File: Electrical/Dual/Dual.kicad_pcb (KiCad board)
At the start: 2 copper layers, 140 x 70 mm, 190 parts, among them J101 01x04, J102 02x04, J103 01x04, J104 01x03, J105 01x03, J106 01x03, J107 01x03, J108 01x03, J109 01x03, J110 01x04, J111 01x04, J112 01x04, J113 01x04, J114 01x03, J115 01x03, J116 01x03, J117 01x03, J201 01x03, J202 01x04, J203 01x03, J204 01x04, J205 01x03, J206 USB_OTG, J207 01x04, J208 01x02, J209 01x04, J210 01x02, J211 01x02, J212 4PostTerm, J213 2PostTerm, J214 2PostTerm, J215 2PostTerm, J216 2PostTerm, J217 2PostTerm, J218 01x02, J219 01x02, Q201 FDC6420C, Q202 FDG1024NZ, Q301 FDC6420C, Q401 FDC6420C, U201 TPD4S012, U202 ACS712ELCTR-05B-T, U203 ACS712ELCTR-05B-T, U204 24LC256, U205 LM2576HVS-ADJ, U206 LM2576HVS-ADJ, x100 02x05, x101 RoutaCell, x102 RoutaCell, x103 RoutaCell, x104 RoutaCell, x105 RoutaCell, x106 RoutaCell, x107 RoutaCell, x108 RoutaCell, x109 RoutaCell, x110 RoutaCell, x111 RoutaCell, x112 RoutaCell, x113 RoutaCell, x114 RoutaCell, x115 RoutaCell, x116 RoutaCell, x117 RoutaCell, x118 RoutaCell, x119 RoutaCell, x120 RoutaCell, x121 RoutaCell, x122 RoutaCell, x123 RoutaCell, x124 RoutaCell, x125 RoutaCell, x126 RoutaCell, x127 RoutaCell, x128 RoutaCell, x129 RoutaCell, x130 RoutaCell, x131 RoutaCell, x132 RoutaCell, x133 RoutaCell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

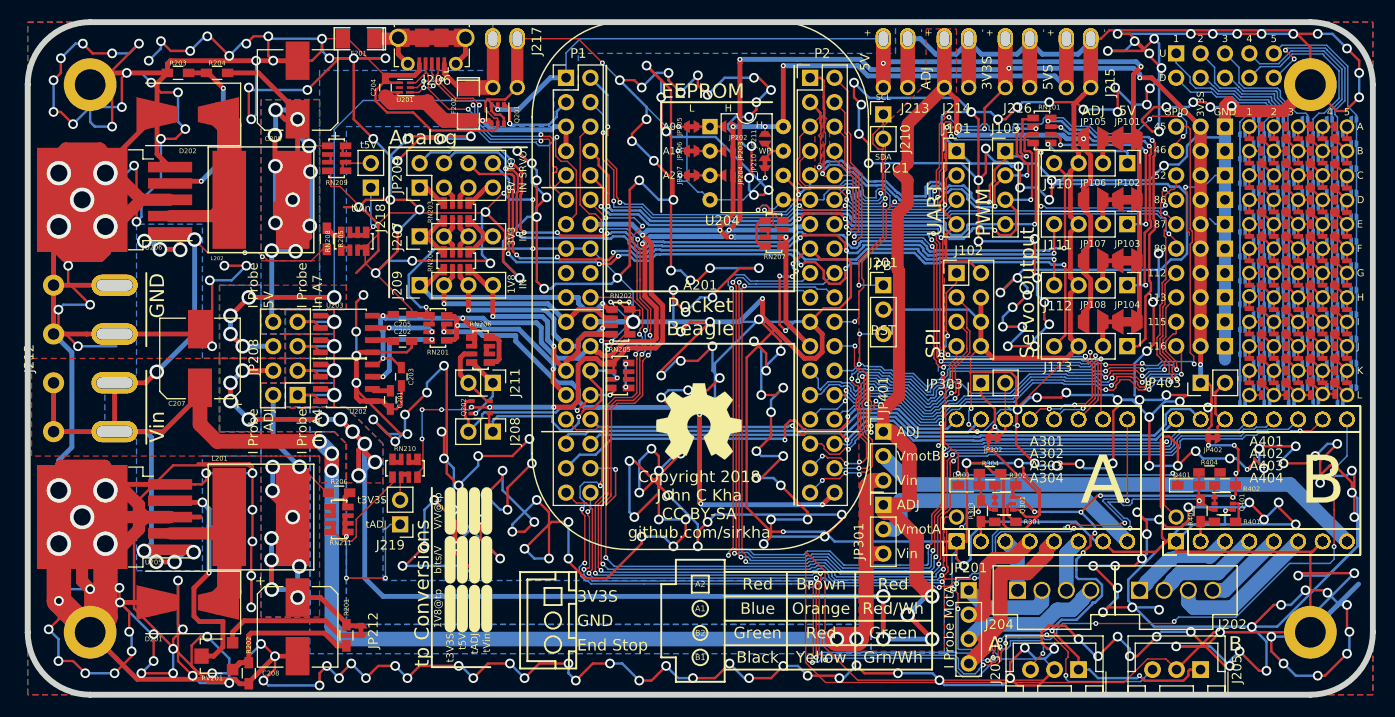
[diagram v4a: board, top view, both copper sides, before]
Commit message: Applied improvements from routing quad board to dual board.
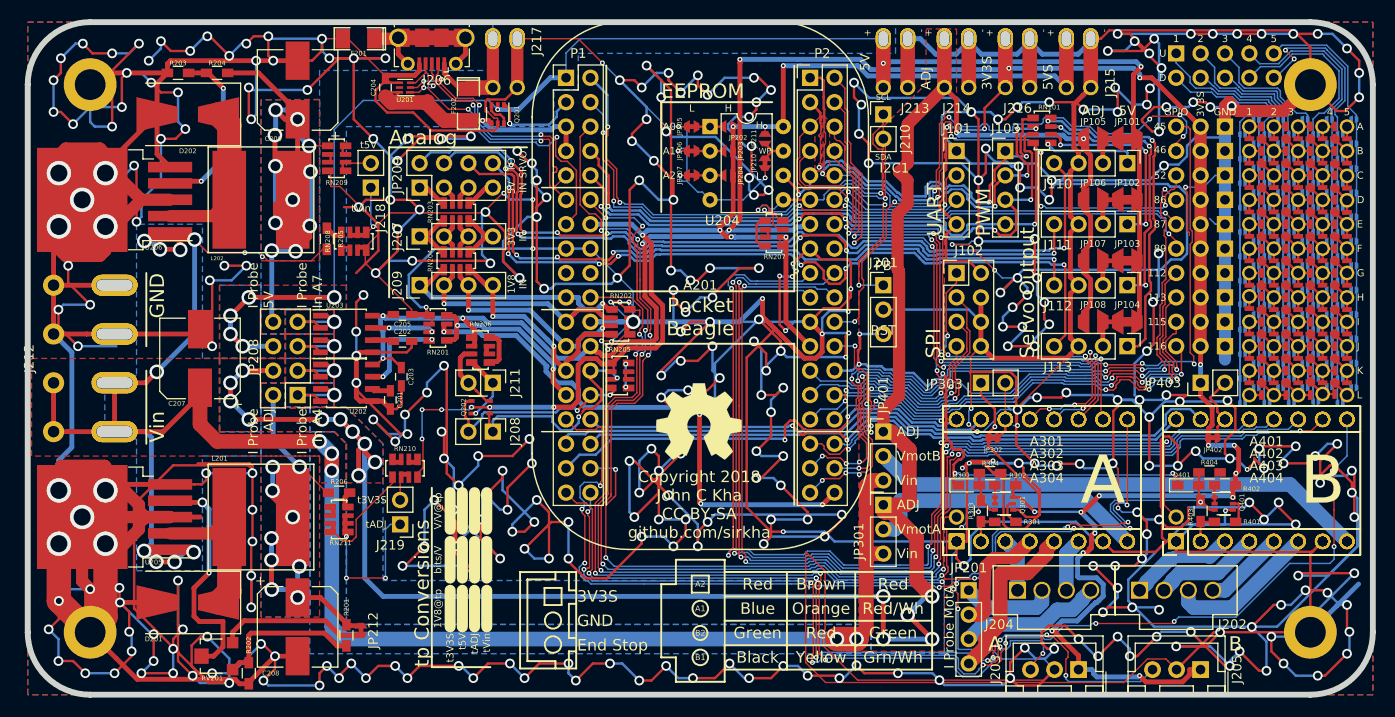
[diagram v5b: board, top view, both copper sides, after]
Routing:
- net GND: track 2759.2 -> 2815.3 mm, vias 381 -> 391
- net RST: track 55.5 -> 64.3 mm
- net 3V3S: track 316.8 -> 325.4 mm, vias 31 -> 30
- net /gpio1_20: track 59.9 -> 58.2 mm
- net /Common/pr1_pru0_pru_r30_07: track 100.9 -> 99.2 mm
- net /Common/i2c1_scl: track 32.0 -> 30.6 mm
- net /spi1_sclk: track 28.8 -> 27.6 mm
- net /spi1_d0: track 23.5 -> 22.3 mm
- net /gpio3_20: track 44.2 -> 43.1 mm
- net /Common/ain3: track 26.5 -> 25.4 mm
- net /Common/gpio0_4: track 126.6 -> 125.5 mm
- net /spi1_d1: track 28.7 -> 29.8 mm, vias 2 -> 3
- net /Common/i2c1_sda: track 26.4 -> 25.5 mm
- net /Common/ain2: track 23.9 -> 23.0 mm
- net 5VS: track 134.2 -> 133.3 mm
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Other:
- net class Default: clearance 0.1524 -> 0.152146
- net class Minimum: clearance 0.1524 -> 0.152146
- net class PowerL: clearance 5.08 -> 0.152146
- net class PowerM: clearance 2.54 -> 0.152146
- net class PowerS: clearance 1.524 -> 0.152146
- rule trace_clearance: 0.1524 -> 0.152146
- rule trace_min: 0.152375 -> 0.14986

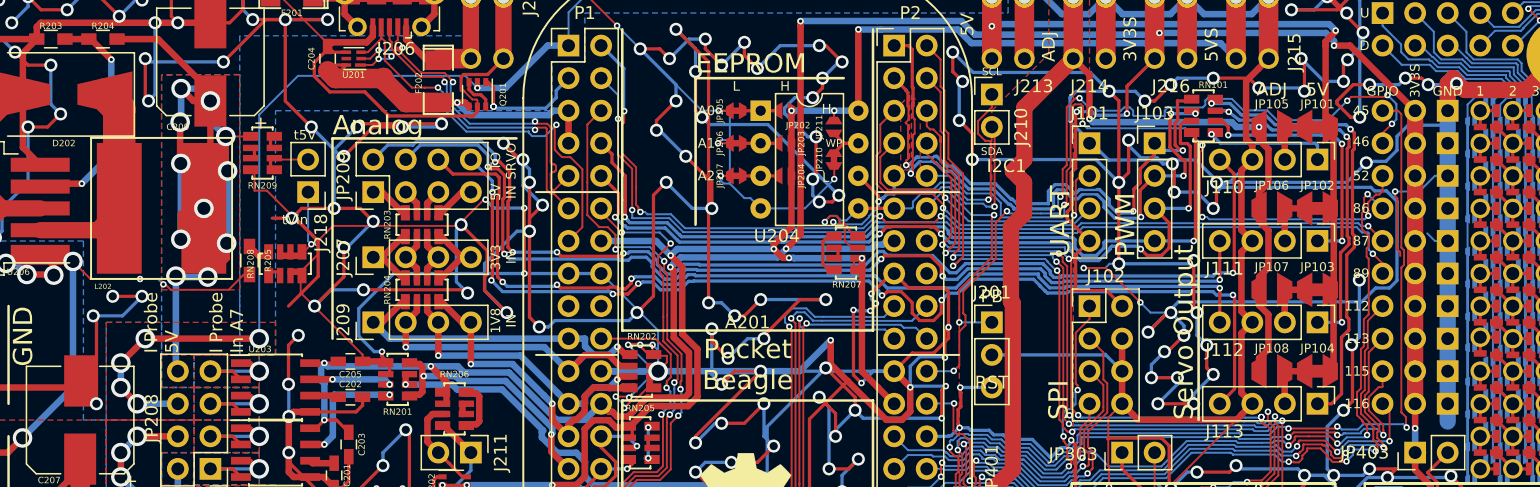
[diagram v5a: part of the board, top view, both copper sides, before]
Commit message: DRC Erros fixed.
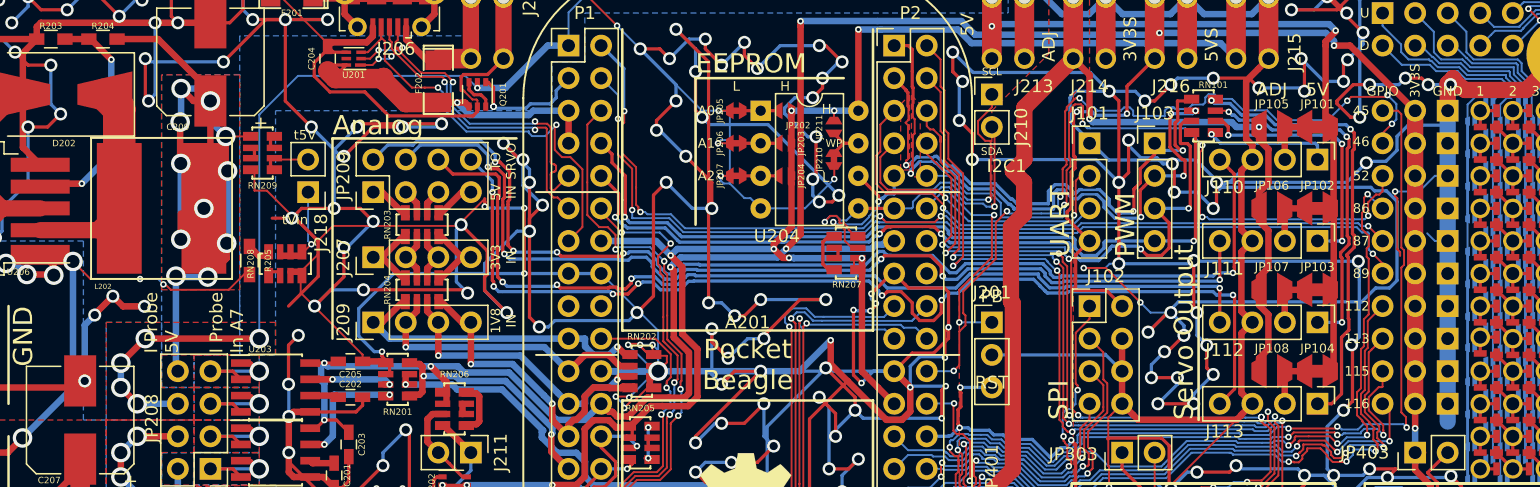
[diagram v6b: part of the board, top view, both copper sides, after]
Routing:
- net GND: track 2815.3 -> 2840.7 mm, vias 391 -> 395
- net (no net): track 13.7 -> 0.00 mm, vias 4 -> 0
- net /gpio1_14: track 62.7 -> 63.5 mm
- net Net-(J112-Pad1): track 29.2 -> 28.4 mm
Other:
- net class Default: clearance 0.152146 -> 0.1524
- net class Minimum: clearance 0.152146 -> 0.1524
- net class PowerL: clearance 0.152146 -> 0.1524
- net class PowerM: clearance 0.152146 -> 0.1524
- net class PowerS: clearance 0.152146 -> 0.1524
- rule trace_clearance: 0.152146 -> 0.1524

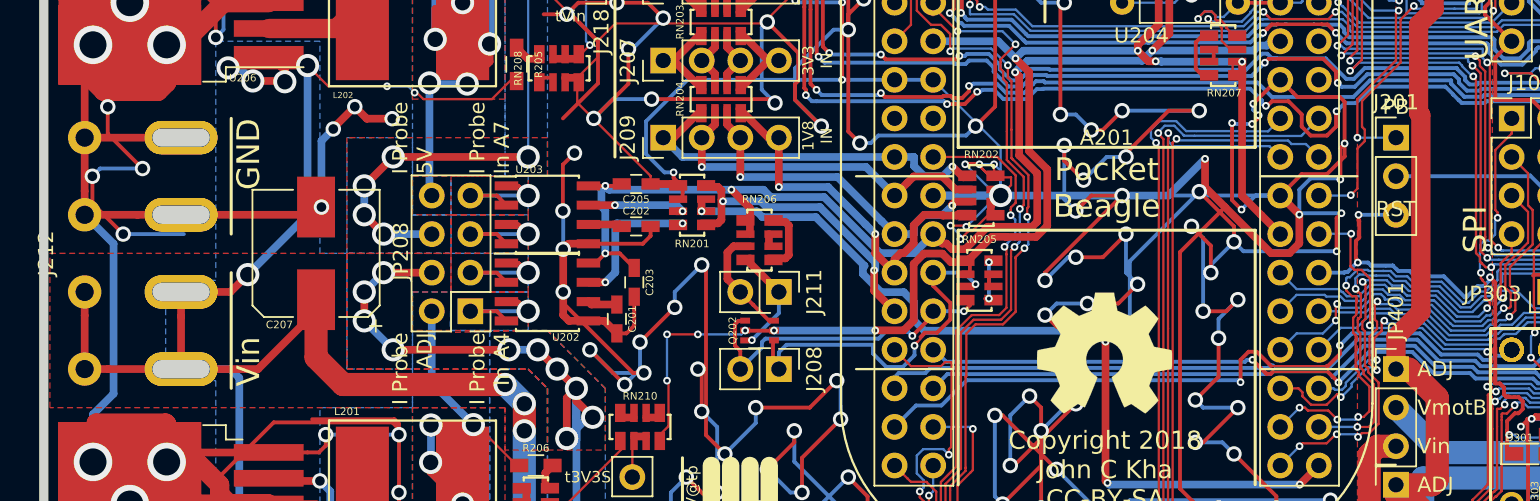
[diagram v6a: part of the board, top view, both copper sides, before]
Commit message: Fixed silkscreen errors and other minor improvements to trace layouts.
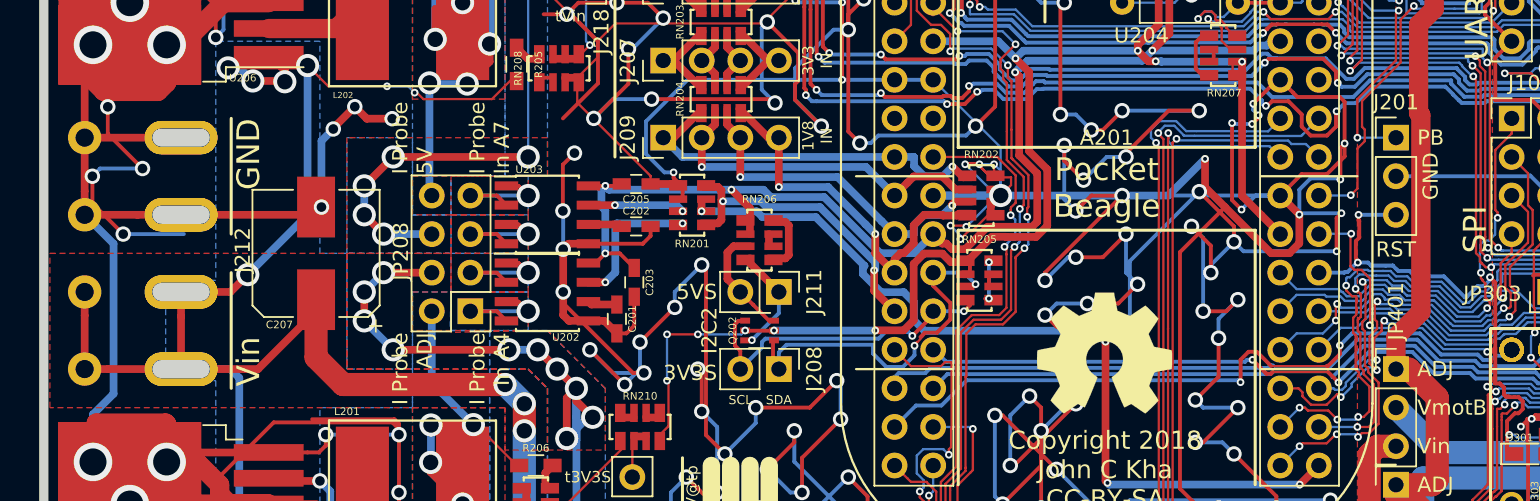
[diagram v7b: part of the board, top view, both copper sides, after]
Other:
- board text added: "I2C2"
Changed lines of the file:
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@@
   (general
     (links 628)
-    (no_connects 0)
-    (area 29.695199 64.695199 170.304801 135.304801)
+    (no_connects 4)
+    (area 13.150001 61.9886 171.057639 147.700001)
     (thickness 1.6)
-    (drawings 284)
+    (drawings 290)
     (tracks 5789)
     (zones 0)
@@
   )
   (setup
-    (last_trace_width 0.1524)
+    (last_trace_width 0.254)
     (user_trace_width 0.1524)
     (user_trace_width 0.254)
@@
   (module footprints:TerminalBlock_Custom_1x04P5.08mm (layer F.Cu)
     (at 36.5 100 270)
-    (fp_text reference J212 (at 0 6.35 270) (layer F.SilkS)
+    (fp_text reference J212 (at -0.21844 -6.604 270) (layer F.SilkS)
       (effects (font (size 1 1) (thickness 0.15)))
     )
@@
     )
   )
+  (gr_text 5VS (at 74.346 102.54) (layer F.SilkS)
+    (effects (font (size 1 1) (thickness 0.2)) (justify right))
+  )
+  (gr_text 3V3S (at 74.346 107.874) (layer F.SilkS)
+    (effects (font (size 1 1) (thickness 0.2)) (justify right))
+  )
+  (gr_text SCL (at 75.87 109.652) (layer F.SilkS)
+    (effects (font (size 0.6 0.6) (thickness 0.15)))
+  )
+  (gr_text SDA (at 78.41 109.652) (layer F.SilkS)
+    (effects (font (size 0.6 0.6) (thickness 0.15)))
+  )
+  (gr_text I2C2 (at 73.838 105.08 90) (layer F.SilkS)
+    (effects (font (size 1 1) (thickness 0.2)))
+  )
+  (gr_text GND (at 121.336 94.92 90) (layer F.SilkS)
+    (effects (font (size 1 1) (thickness 0.2)))
+  )
   (gr_text "Prototyping area inspired by Routaboard.\nroutaboard.com" (at 168.834 110.414) (layer B.SilkS)
     (effects (font (size 1.5 1.5) (thickness 0.3)) (justify left mirror))
@@
     (effects (font (size 0.6 0.6) (thickness 0.15)))
   )
-  (gr_text PB (at 119.05 90.348) (layer F.SilkS)
+  (gr_text PB (at 121.336 92.38) (layer F.SilkS)
     (effects (font (size 1 1) (thickness 0.2)))
   )
@@
   )
   (gr_line (start 135.179 100) (end 135.179 78.41) (layer F.SilkS) (width 0.2))
-  (gr_text RST (at 119.05 97.079) (layer F.SilkS)
+  (gr_text RST (at 119.05 99.746) (layer F.SilkS)
     (effects (font (size 1 1) (thickness 0.2)))
   )
@@
     (connect_pads (clearance 0.25146))
     (min_thickness 0.25146)
-    (fill yes (arc_segments 16) (thermal_gap 0.254) (thermal_bridge_width 1.524))
+    (fill (arc_segments 16) (thermal_gap 0.254) (thermal_bridge_width 1.524))
     (polygon
       (pts
@@
     (connect_pads (clearance 0.25146))
     (min_thickness 0.25146)
-    (fill yes (arc_segments 16) (thermal_gap 0.254) (thermal_bridge_width 1.524))
+    (fill (arc_segments 16) (thermal_gap 0.254) (thermal_bridge_width 1.524))
     (polygon
       (pts
@@
     (connect_pads (clearance 0.25146))
     (min_thickness 0.25146)
-    (fill yes (arc_segments 16) (thermal_gap 0.254) (thermal_bridge_width 1.524))
+    (fill (arc_segments 16) (thermal_gap 0.254) (thermal_bridge_width 1.524))
     (polygon
       (pts
@@
     (connect_pads (clearance 0.25146))
     (min_thickness 0.25146)
-    (fill yes (arc_segments 16) (thermal_gap 0.254) (thermal_bridge_width 1.524))
+    (fill (arc_segments 16) (thermal_gap 0.254) (thermal_bridge_width 1.524))
     (polygon
       (pts
@@
     (connect_pads (clearance 0.25146))
     (min_thickness 0.25146)
-    (fill yes (arc_segments 16) (thermal_gap 0.254) (thermal_bridge_width 1.524))
+    (fill (arc_segments 16) (thermal_gap 0.254) (thermal_bridge_width 1.524))
     (polygon
       (pts
@@
     (connect_pads (clearance 0.25146))
     (min_thickness 0.25146)
-    (fill yes (arc_segments 16) (thermal_gap 0.254) (thermal_bridge_width 1.524))
+    (fill (arc_segments 16) (thermal_gap 0.254) (thermal_bridge_width 1.524))
     (polygon
       (pts
@@
     (connect_pads (clearance 0.1778))
     (min_thickness 0.1778)
-    (fill yes (arc_segments 16) (thermal_gap 0.254) (thermal_bridge_width 0.254))
+    (fill (arc_segments 16) (thermal_gap 0.254) (thermal_bridge_width 0.254))
     (polygon
       (pts
@@
     (connect_pads (clearance 0.1778))
     (min_thickness 0.1778)
-    (fill yes (arc_segments 16) (thermal_gap 0.254) (thermal_bridge_width 0.254))
+    (fill (arc_segments 16) (thermal_gap 0.254) (thermal_bridge_width 0.254))
     (polygon
       (pts
@@
     (connect_pads (clearance 0.25146))
     (min_thickness 0.25146)
-    (fill yes (arc_segments 16) (thermal_gap 0.254) (thermal_bridge_width 1.524))
+    (fill (arc_segments 16) (thermal_gap 0.254) (thermal_bridge_width 1.524))
     (polygon
       (pts
@@
     (connect_pads (clearance 0.25146))
     (min_thickness 0.25146)
-    (fill yes (arc_segments 16) (thermal_gap 0.254) (thermal_bridge_width 1.524))
+    (fill (arc_segments 16) (thermal_gap 0.254) (thermal_bridge_width 1.524))
     (polygon
       (pts
@@
     (connect_pads (clearance 0.25146))
     (min_thickness 0.25146)
-    (fill yes (arc_segments 16) (thermal_gap 0.254) (thermal_bridge_width 1.524))
+    (fill (arc_segments 16) (thermal_gap 0.254) (thermal_bridge_width 1.524))
     (polygon
       (pts
@@
     (connect_pads (clearance 0.25146))
     (min_thickness 0.25146)
-    (fill yes (arc_segments 16) (thermal_gap 0.254) (thermal_bridge_width 1.524))
+    (fill (arc_segments 16) (thermal_gap 0.254) (thermal_bridge_width 1.524))
     (polygon
       (pts
@@
     (connect_pads (clearance 0.25146))
     (min_thickness 0.25146)
-    (fill yes (arc_segments 16) (thermal_gap 0.254) (thermal_bridge_width 1.524))
+    (fill (arc_segments 16) (thermal_gap 0.254) (thermal_bridge_width 1.524))
     (polygon
       (pts
@@
     (connect_pads (clearance 0.25146))
     (min_thickness 0.25146)
-    (fill yes (arc_segments 16) (thermal_gap 0.254) (thermal_bridge_width 1.524))
+    (fill (arc_segments 16) (thermal_gap 0.254) (thermal_bridge_width 1.524))
     (polygon
       (pts
@@
     (connect_pads (clearance 0.25146))
     (min_thickness 0.25146)
-    (fill yes (arc_segments 16) (thermal_gap 0.254) (thermal_bridge_width 1.524))
+    (fill (arc_segments 16) (thermal_gap 0.254) (thermal_bridge_width 1.524))
     (polygon
       (pts
@@
     (connect_pads (clearance 0.25146))
     (min_thickness 0.25146)
-    (fill yes (arc_segments 16) (thermal_gap 0.254) (thermal_bridge_width 1.524))
+    (fill (arc_segments 16) (thermal_gap 0.254) (thermal_bridge_width 1.524))
     (polygon
       (pts
@@
     (connect_pads (clearance 0.25146))
     (min_thickness 0.25146)
-    (fill yes (arc_segments 16) (thermal_gap 0.254) (thermal_bridge_width 1.524))
+    (fill (arc_segments 16) (thermal_gap 0.254) (thermal_bridge_width 1.524))
     (polygon
       (pts
@@
     (connect_pads (clearance 0.25146))
     (min_thickness 0.25146)
-    (fill yes (arc_segments 16) (thermal_gap 0.254) (thermal_bridge_width 1.524))
+    (fill (arc_segments 16) (thermal_gap 0.254) (thermal_bridge_width 1.524))
     (polygon
       (pts
@@
     (connect_pads (clearance 0.25146))
     (min_thickness 0.25146)
-    (fill yes (arc_segments 16) (thermal_gap 0.254) (thermal_bridge_width 1.524))
+    (fill (arc_segments 16) (thermal_gap 0.254) (thermal_bridge_width 1.524))
     (polygon
       (pts
@@
     (connect_pads (clearance 0.25146))
     (min_thickness 0.25146)
-    (fill yes (arc_segments 16) (thermal_gap 0.254) (thermal_bridge_width 1.524))
+    (fill (arc_segments 16) (thermal_gap 0.254) (thermal_bridge_width 1.524))
     (polygon
       (pts
@@
     (connect_pads (clearance 0.25146))
     (min_thickness 0.25146)
-    (fill yes (arc_segments 16) (thermal_gap 0.254) (thermal_bridge_width 1.524))
+    (fill (arc_segments 16) (thermal_gap 0.254) (thermal_bridge_width 1.524))
     (polygon
       (pts
@@
     (connect_pads (clearance 0.25146))
     (min_thickness 0.25146)
-    (fill yes (arc_segments 16) (thermal_gap 0.254) (thermal_bridge_width 1.524))
+    (fill (arc_segments 16) (thermal_gap 0.254) (thermal_bridge_width 1.524))
     (polygon
       (pts
@@
     (connect_pads (clearance 0.25146))
     (min_thickness 0.25146)
-    (fill yes (arc_segments 16) (thermal_gap 0.254) (thermal_bridge_width 1.524))
+    (fill (arc_segments 16) (thermal_gap 0.254) (thermal_bridge_width 1.524))
     (polygon
       (pts
@@
     (connect_pads (clearance 0.1778))
     (min_thickness 0.1778)
-    (fill yes (arc_segments 16) (thermal_gap 0.254) (thermal_bridge_width 0.254))
+    (fill (arc_segments 16) (thermal_gap 0.254) (thermal_bridge_width 0.254))
     (polygon
       (pts
@@
     (connect_pads (clearance 0.1524))
     (min_thickness 0.1524)
-    (fill yes (arc_segments 16) (thermal_gap 0.254) (thermal_bridge_width 0.254))
+    (fill (arc_segments 16) (thermal_gap 0.254) (thermal_bridge_width 0.254))
     (polygon
       (pts
@@
     (connect_pads (clearance 0.1524))
     (min_thickness 0.1524)
-    (fill yes (arc_segments 16) (thermal_gap 0.254) (thermal_bridge_width 0.254))
+    (fill (arc_segments 16) (thermal_gap 0.254) (thermal_bridge_width 0.254))
     (polygon
       (pts
